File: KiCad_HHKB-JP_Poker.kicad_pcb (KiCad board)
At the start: 2 copper layers, 285 x 95.1 mm, 153 parts, among them SW1 SW_Push, U1 ATmega32U4-MU, U2 PRTR5V0U2X, Y1 16MHz

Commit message: Save Point 2 (Remove ai03's logos)
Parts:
- removed G*** (x2): LOGO, locallib:ai-ring-6mm-Combined
- removed K_SPC1: MX-NoLED, MX_Only:MXOnly-6U-Centered-Hotswap-ReversedStabilizers
- removed K_SPC2: MX-NoLED, MX_Only:MXOnly-1U-Hotswap
- added D10: SOD-123, Diode_SMD:D_SOD-123, F.Cu at (311.1, 295.4)
- added D11: SOD-123, Diode_SMD:D_SOD-123, F.Cu at (290.9, 312.3)
- added D37: SOD-123, Diode_SMD:D_SOD-123, F.Cu at (296.7, 312.3)
- added D42: SOD-123, Diode_SMD:D_SOD-123, F.Cu at (290.9, 315.6)
- added D43: SOD-123, Diode_SMD:D_SOD-123, F.Cu at (311.1, 292.1)
- added K_HENK1: MX-NoLED, MX_Only:MXOnly-1U-Hotswap, F.Cu at (298.2, 300.5)
- added K_LSPACE1: MX-NoLED, MX_Only:MXOnly-1.25U-Hotswap, F.Cu at (255.4, 320.7)
- added K_RSPACE1: MX-NoLED, MX_Only:MXOnly-1.25U-Hotswap, F.Cu at (255.4, 300.5)
- added K_UP1: MX-NoLED, MX_Only:MXOnly-1U-Hotswap, F.Cu at (278.0, 300.5)
- added K_WIN1: MX-NoLED, MX_Only:MXOnly-1U-Hotswap, F.Cu at (278.0, 320.7)
- K_LCTRL1: footprint MX_Only:MXOnly-1.25U-Hotswap -> MX_Only:MXOnly-1U-Hotswap
- K_LSFT1: footprint MX_Only:MXOnly-2.25U-Hotswap -> MX_Only:MXOnly-2U-Hotswap
- K_NHENK1: renamed from K_NFER1; footprint MX_Only:MXOnly-1.25U-Hotswap -> MX_Only:MXOnly-1U-Hotswap
- K_RSFT1: renamed from K_SRSFT2; footprint MX_Only:MXOnly-1.75U-Hotswap -> MX_Only:MXOnly-1U-Hotswap
- REF**: footprint locallib:60_Outline-Modded-Extreme -> locallib:60_Outline-Modded-Extreme-deleteCenterHole
- renumbered K_RGUI1 to K_DOWN1, K_RALT1 to K_LEFT1, K_\1 to K_PIPE1, K_RCTRL1 to K_RIGHT1, K_SRSFT1 to K_UNSC1
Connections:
- K_,1 pad 1: COL9 -> COL8
- K_.1 pad 1: COL10 -> COL9
- K_/1 pad 1: COL11 -> COL10
- K_B1 pad 1: COL6 -> COL5
- K_C1 pad 1: COL4 -> COL3
- K_M1 pad 1: COL8 -> COL7
- K_N1 pad 1: COL7 -> COL6
- K_UNSC1 pad 1: COL12 -> COL11
- K_V1 pad 1: COL5 -> COL4
- K_X1 pad 1: COL3 -> COL2
- K_Z1 pad 1: COL2 -> COL1
- REF** pad 1: Earth -> (no net)
- U1 pad 10: Net-(U1-Pad10) -> unconnected-(U1-Pad10)
- U1 pad 11: Net-(U1-Pad11) -> unconnected-(U1-Pad11)
- U1 pad 12: Net-(U1-Pad12) -> unconnected-(U1-Pad12)
- U1 pad 18: Net-(U1-Pad18) -> unconnected-(U1-Pad18)
- U1 pad 42: Net-(U1-Pad42) -> unconnected-(U1-Pad42)
- U1 pad 8: Net-(U1-Pad8) -> unconnected-(U1-Pad8)
- U1 pad 9: Net-(U1-Pad9) -> unconnected-(U1-Pad9)
- USB1 pad 3: Net-(USB1-Pad3) -> unconnected-(USB1-Pad3)
- USB1 pad 9: Net-(USB1-Pad9) -> unconnected-(USB1-Pad9)
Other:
- net class Default removed
- net class Earth removed
- net class Power removed
- net class USB removed
- board text removed: "JP60"
- board text removed: "JP60 R1.0 20210717 | ai03.com"

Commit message: Save Point 3 (Remove F:Cu on R4)
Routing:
- net COL12: track 281.0 -> 220.2 mm, vias 7 -> 6
- net ROW4: track 328.0 -> 276.4 mm
- net COL0: track 189.4 -> 147.2 mm
- net COL11: track 219.6 -> 177.5 mm
- net COL10: track 196.9 -> 155.9 mm
- net COL2: track 162.4 -> 121.7 mm
- net COL7: track 143.0 -> 102.9 mm
- net COL3: track 142.0 -> 102.5 mm
- net COL1: track 172.9 -> 134.7 mm, vias 6 -> 7
- net COL8: track 140.6 -> 105.0 mm
- net COL9: track 159.1 -> 124.1 mm
- net COL13: track 293.5 -> 261.0 mm
- net +5V: track 200.6 -> 170.9 mm
- net COL4: track 110.8 -> 82.0 mm
- net GND: track 255.4 -> 227.6 mm
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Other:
- board text added: "2U"
- board text removed: "2.25U"
- board text removed: "6U-CENTERED"
- board text removed: "6U-OFFCENTER"

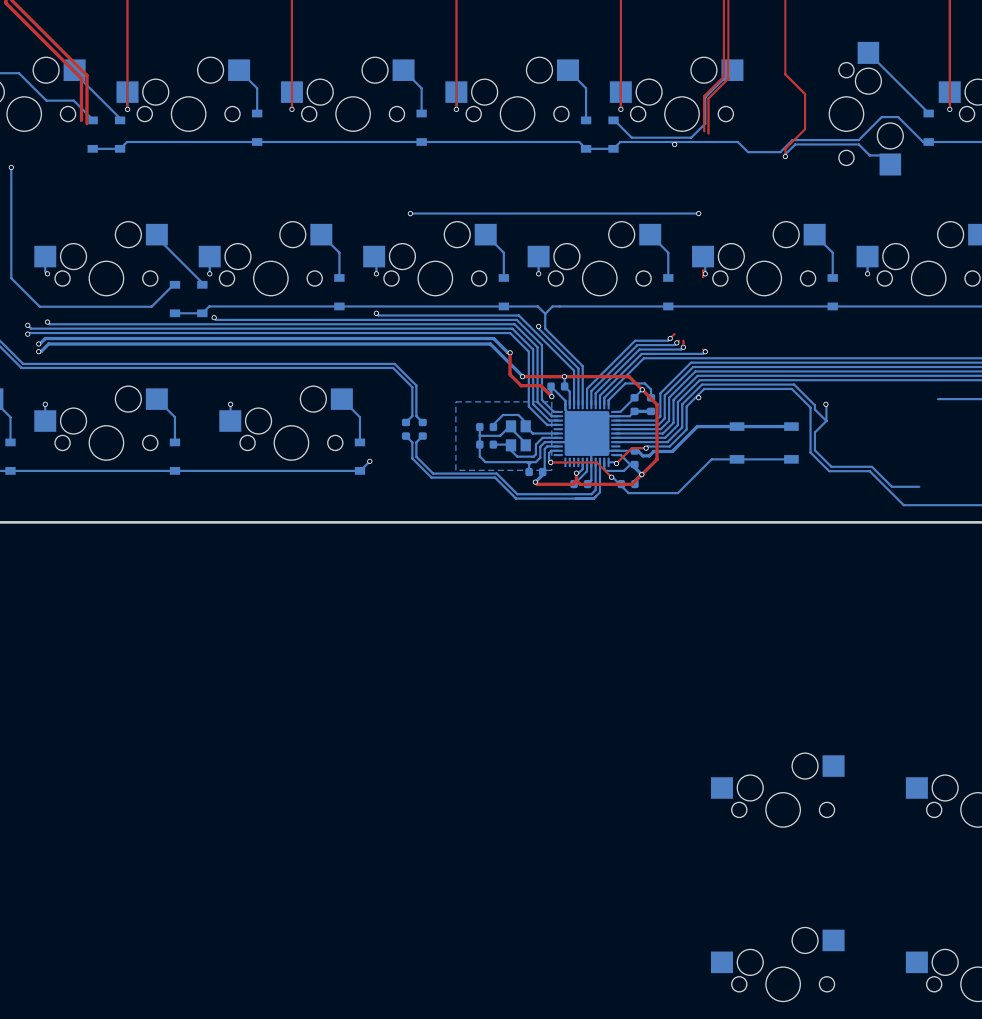
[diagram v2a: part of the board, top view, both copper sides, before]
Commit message: Save Point4 (Move MCU)
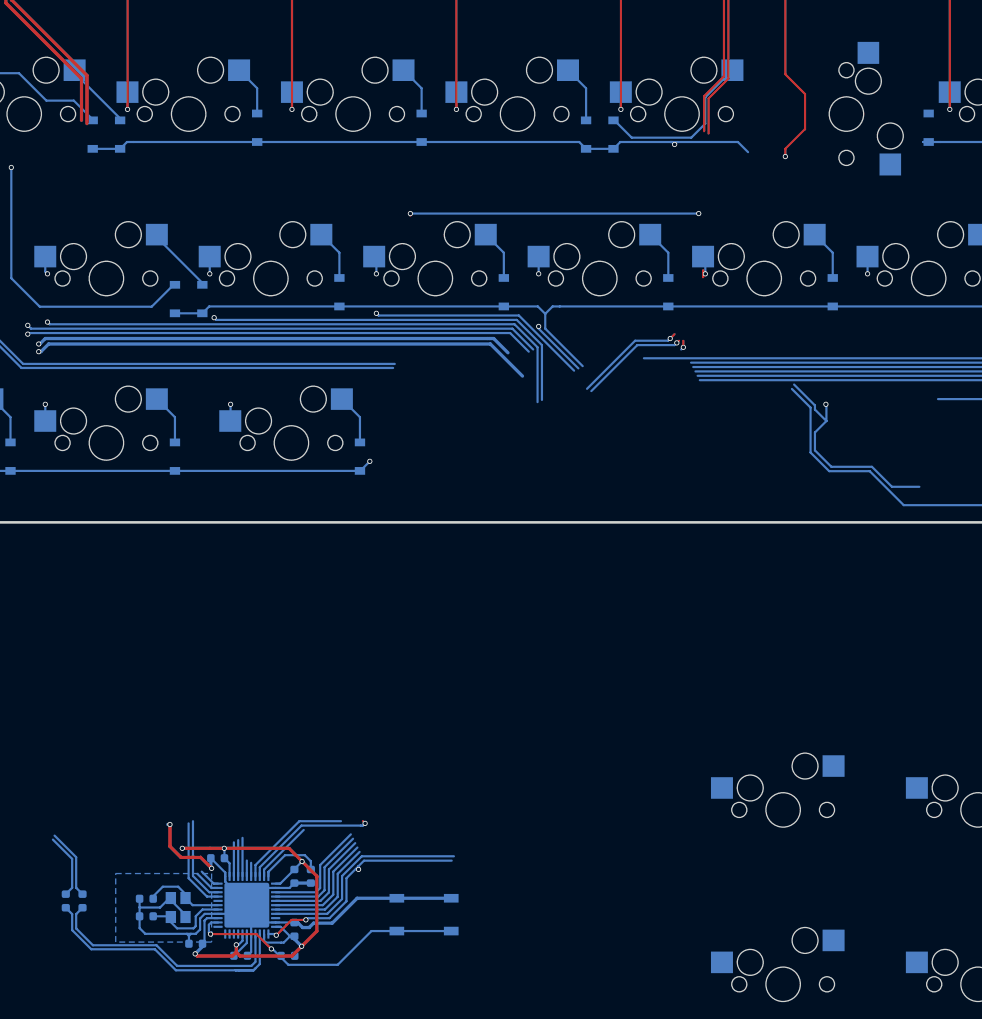
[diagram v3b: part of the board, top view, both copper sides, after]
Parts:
- moved C2 67.4 mm to (198.8, 308.2)
- moved C4 67.4 mm to (198.8, 314.3)
- moved R3 67.4 mm to (172.3, 311.0)
- moved R4 67.4 mm to (200.7, 308.2)
- moved SW1 67.4 mm to (213.8, 312.6)
- moved U1 67.4 mm to (193.3, 311.5)
- moved C1 67.4 mm to (189.9, 306.1)
- moved C3 67.4 mm to (187.4, 316.0)
- moved C5 67.4 mm to (181.6, 310.8)
- moved C6 67.4 mm to (181.6, 312.8)
- moved C7 67.4 mm to (192.6, 317.4)
- moved R1 67.4 mm to (174.2, 311.0)
- moved R5 67.4 mm to (198.0, 317.4)
- moved Y1 67.4 mm to (185.3, 311.8)
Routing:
- net ROW2: track 293.3 -> 270.2 mm
- net COL6: track 87.3 -> 75.2 mm
- net Net-(D35-Pad2): track 9.92 -> 0.04 mm

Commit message: Save Point 5 (Remove B:Cu on R4)
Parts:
- moved D42 26.9 mm to (292.4, 286.1)
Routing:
- net ROW4: track 276.4 -> 62.2 mm
- net ROW3: track 207.0 -> 5.59 mm
- net COL13: track 261.0 -> 104.4 mm
- net COL12: track 220.2 -> 90.8 mm
- net COL11: track 177.5 -> 67.6 mm
- net COL0: track 147.2 -> 50.3 mm, vias 7 -> 4
- net COL10: track 155.9 -> 67.9 mm
- net D-: track 134.9 -> 54.8 mm
- net D+: track 135.2 -> 55.5 mm
- net COL1: track 134.7 -> 65.6 mm, vias 7 -> 5
- net COL2: track 121.7 -> 57.4 mm, vias 6 -> 5
- net +5V: track 170.9 -> 113.0 mm, vias 8 -> 7
- net COL9: track 124.1 -> 66.2 mm, vias 5 -> 4
- net GND: track 227.6 -> 172.3 mm, vias 6 -> 5
- net COL3: track 102.5 -> 57.2 mm
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
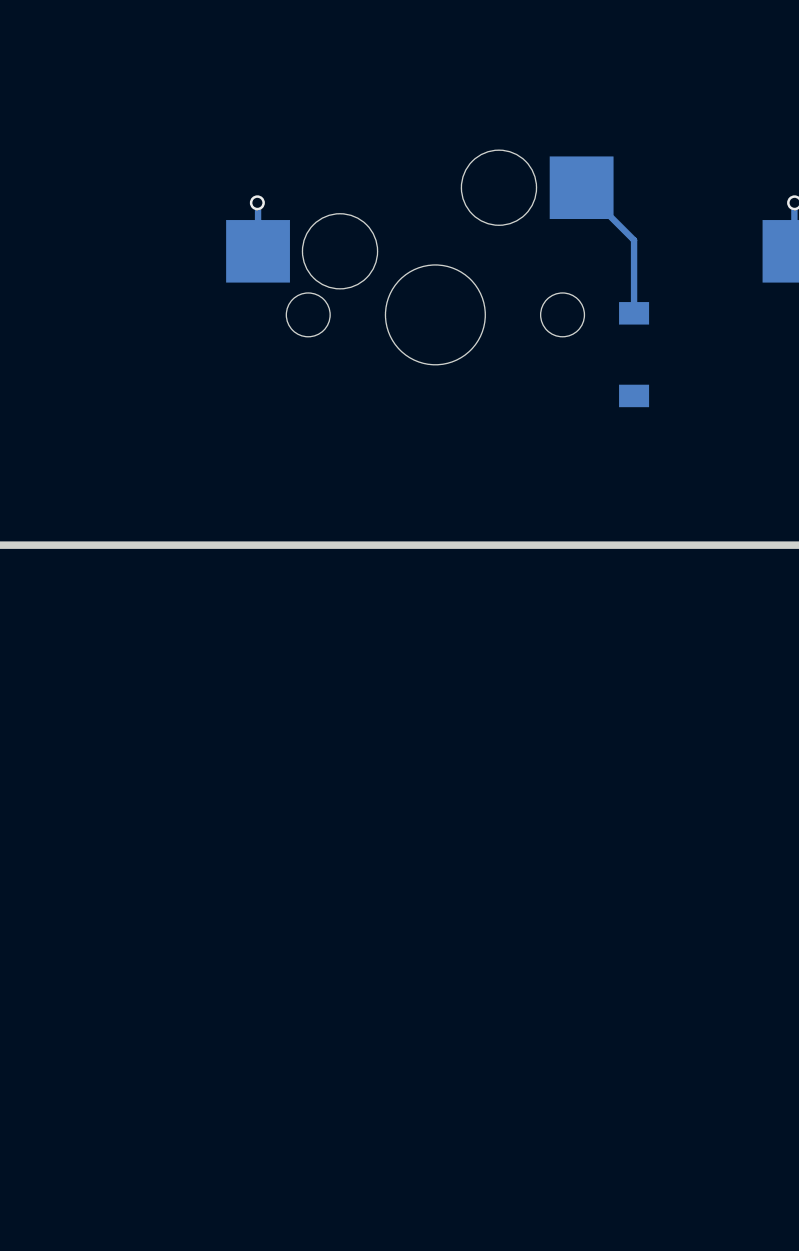
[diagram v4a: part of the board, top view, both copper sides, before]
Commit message: Correct Symbol Names (bkspとかの辺)
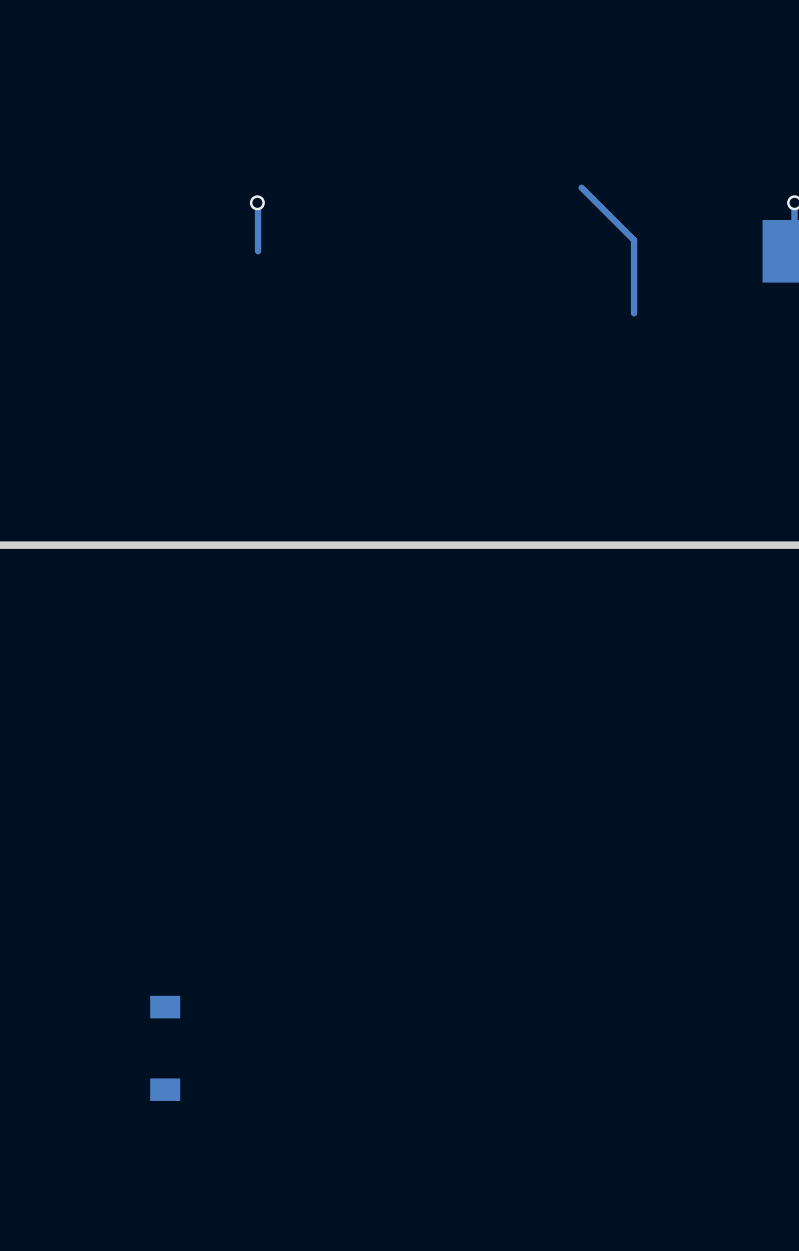
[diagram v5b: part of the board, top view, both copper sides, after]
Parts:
- removed K_XFER1: MX-NoLED, MX_Only:MXOnly-1.25U-Hotswap
- moved D10 33.5 mm to (325.8, 287.3)
- renumbered K_'1 to K_:1, K_[1 to K_@1, K_SBSPC2 to K_BKSPC1, K_SBSPC1 to K_PIPE1, K_]1 to K_[1, K_PIPE1 to K_]2
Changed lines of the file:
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@@
     (property "Sheetname" "matrix")
     (attr smd)
-    (fp_text reference "K_'1" (at 0 3.175) (layer "B.Fab")
+    (fp_text reference "K_:1" (at 0 3.175) (layer "B.Fab")
       (effects (font (size 1 1) (thickness 0.15)) (justify mirror))
     )
@@
     (property "Sheetname" "matrix")
     (attr smd)
-    (fp_text reference "K_[1" (at 0 3.175) (layer "B.Fab")
+    (fp_text reference "K_@1" (at 0 3.175) (layer "B.Fab")
       (effects (font (size 1 1) (thickness 0.15)) (justify mirror))
     )
@@
     (property "Sheetname" "matrix")
     (attr smd)
-    (fp_text reference "K_PIPE1" (at 0 3.175) (layer "B.Fab")
+    (fp_text reference "K_]2" (at 0 3.175) (layer "B.Fab")
       (effects (font (size 1 1) (thickness 0.15)) (justify mirror))
     )
@@
     (property "Sheetname" "matrix")
     (attr smd)
-    (fp_text reference "K_]1" (at 0 3.175) (layer "B.Fab")
+    (fp_text reference "K_[1" (at 0 3.175) (layer "B.Fab")
       (effects (font (size 1 1) (thickness 0.15)) (justify mirror))
     )
@@
     (property "Sheetname" "matrix")
     (attr smd)
-    (fp_text reference "K_SBSPC1" (at 0 3.175) (layer "B.Fab")
+    (fp_text reference "K_PIPE1" (at 0 3.175) (layer "B.Fab")
       (effects (font (size 1 1) (thickness 0.15)) (justify mirror))
     )
@@
     (property "Sheetname" "matrix")
     (attr smd)
-    (fp_text reference "K_SBSPC2" (at 0 3.175) (layer "B.Fab")
+    (fp_text reference "K_BKSPC1" (at 0 3.175) (layer "B.Fab")
       (effects (font (size 1 1) (thickness 0.15)) (justify mirror))
     )
@@
     )
   )
-  (footprint "MX_Only:MXOnly-1.25U-Hotswap" (layer "F.Cu")
-    (at 336.55 257.96875)
-    (attr smd)
-    (fp_text reference "K_XFER1" (at 0 3.048) (layer "B.Fab")
-      (effects (font (size 1 1) (thickness 0.15)) (justify mirror))
-    )
-    (fp_text value "MX-NoLED" (at 0 -7.9375) (layer "Dwgs.User")
-      (effects (font (size 1 1) (thickness 0.15)))
-    )
-    (fp_line (start -11.90625 9.525) (end -11.90625 -9.525) (layer "Dwgs.User") (width 0.15))
-    (fp_line (start 7 -7) (end 7 -5) (layer "Dwgs.User") (width 0.15))
-    (fp_line (start 11.90625 -9.525) (end 11.90625 9.525) (layer "Dwgs.User") (width 0.15))
-    (fp_line (start 5 -7) (end 7 -7) (layer "Dwgs.User") (width 0.15))
-    (fp_line (start 11.90625 9.525) (end -11.90625 9.525) (layer "Dwgs.User") (width 0.15))
-    (fp_line (start -7 -7) (end -7 -5) (layer "Dwgs.User") (width 0.15))
-    (fp_line (start 7 7) (end 7 5) (layer "Dwgs.User") (width 0.15))
-    (fp_line (start -7 7) (end -5 7) (layer "Dwgs.User") (width 0.15))
-    (fp_line (start -5 -7) (end -7 -7) (layer "Dwgs.User") (width 0.15))
-    (fp_line (start -11.90625 -9.525) (end 11.90625 -9.525) (layer "Dwgs.User") (width 0.15))
-    (fp_line (start -7 5) (end -7 7) (layer "Dwgs.User") (width 0.15))
-    (fp_line (start 5 7) (end 7 7) (layer "Dwgs.User") (width 0.15))
-    (fp_line (start -8.382 -3.81) (end -5.842 -3.81) (layer "B.CrtYd") (width 0.15))
-    (fp_line (start 4.572 -6.35) (end 7.112 -6.35) (layer "B.CrtYd") (width 0.15))
-    (fp_line (start 4.572 -3.81) (end 4.572 -6.35) (layer "B.CrtYd") (width 0.15))
-    (fp_line (start 5.3 -7) (end -4 -7) (layer "B.CrtYd") (width 0.127))
-    (fp_line (start -6.5 -4.5) (end -6.5 -0.6) (layer "B.CrtYd") (width 0.127))
-    (fp_line (start 7.112 -3.81) (end 4.572 -3.81) (layer "B.CrtYd") (width 0.15))
-    (fp_line (start 5.3 -7) (end 5.3 -2.6) (layer "B.CrtYd") (width 0.127))
-    (fp_line (start -6.5 -0.6) (end -2.4 -0.6) (layer "B.CrtYd") (width 0.127))
-    (fp_line (start 7.112 -6.35) (end 7.112 -3.81) (layer "B.CrtYd") (width 0.15))
-    (fp_line (start -0.4 -2.6) (end 5.3 -2.6) (layer "B.CrtYd") (width 0.127))
-    (fp_line (start -8.382 -1.27) (end -8.382 -3.81) (layer "B.CrtYd") (width 0.15))
-    (fp_line (start -5.842 -3.81) (end -5.842 -1.27) (layer "B.CrtYd") (width 0.15))
-    (fp_line (start -5.842 -1.27) (end -8.382 -1.27) (layer "B.CrtYd") (width 0.15))
-    (fp_arc (start -2.4 -0.6) (mid -1.814214 -2.014214) (end -0.4 -2.6) (layer "B.CrtYd") (width 0.127))
-    (fp_arc (start -6.5 -4.5) (mid -5.767767 -6.267767) (end -4 -7) (layer "B.CrtYd") (width 0.127))
-    (fp_circle (center 2.54 -5.08) (end 2.54 -6.604) (layer "B.CrtYd") (width 0.15) (fill none))
-    (fp_circle (center -3.81 -2.54) (end -3.81 -4.064) (layer "B.CrtYd") (width 0.15) (fill none))
-    (pad "" np_thru_hole circle locked (at -5.08 0 48.0996) (size 1.75 1.75) (drill 1.75) (layers *.Cu *.Mask))
-    (pad "" np_thru_hole circle locked (at -3.81 -2.54) (size 3 3) (drill 3) (layers *.Cu *.Mask))
-    (pad "" np_thru_hole circle locked (at 5.08 0 48.0996) (size 1.75 1.75) (drill 1.75) (layers *.Cu *.Mask))
-    (pad "" np_thru_hole circle locked (at 0 0) (size 3.9878 3.9878) (drill 3.9878) (layers *.Cu *.Mask))
-    (pad "" np_thru_hole circle locked (at 2.54 -5.08) (size 3 3) (drill 3) (layers *.Cu *.Mask))
-    (pad "1" smd rect locked (at -7.085 -2.54) (size 2.55 2.5) (layers "B.Cu" "B.Paste" "B.Mask")
-      (net 79 "COL10"))
-    (pad "2" smd rect locked (at 5.842 -5.08) (size 2.55 2.5) (layers "B.Cu" "B.Paste" "B.Mask")
-      (net 97 "Net-(D10-Pad2)"))
-    (model "${KILIB}/MX_Alps_Hybrid.pretty/MX_Only.pretty/3d_shapes/CPG151101S11.wrl"
-      (offset (xyz 0 0 -1.4868))
-      (scale (xyz 0.3937 0.3937 0.3937))
-      (rotate (xyz 0 0 0))
-    )
-  )
   (footprint "locallib:60_Outline-Modded-Extreme-deleteCenterHole" locked (layer "F.Cu")
     (at 267.49375 219.86875)
@@
   )
   (footprint "Diode_SMD:D_SOD-123" (layer "B.Cu")
-    (at 344.4875 259.55625 90)
+    (at 325.755 287.275 90)
     (descr "SOD-123")
     (tags "SOD-123")
@@
     (effects (font (size 1 1) (thickness 0.15)) (justify mirror))
   )
-  (gr_text "1.25U" (at 336.55 261.14375) (layer "B.SilkS")
-    (effects (font (size 1 1) (thickness 0.15)) (justify mirror))
-  )
